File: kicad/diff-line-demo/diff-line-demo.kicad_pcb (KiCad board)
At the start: 4 copper layers, 120 x 120 mm, 2 parts, among them J1 HDMI_A, J2 HDMI_A

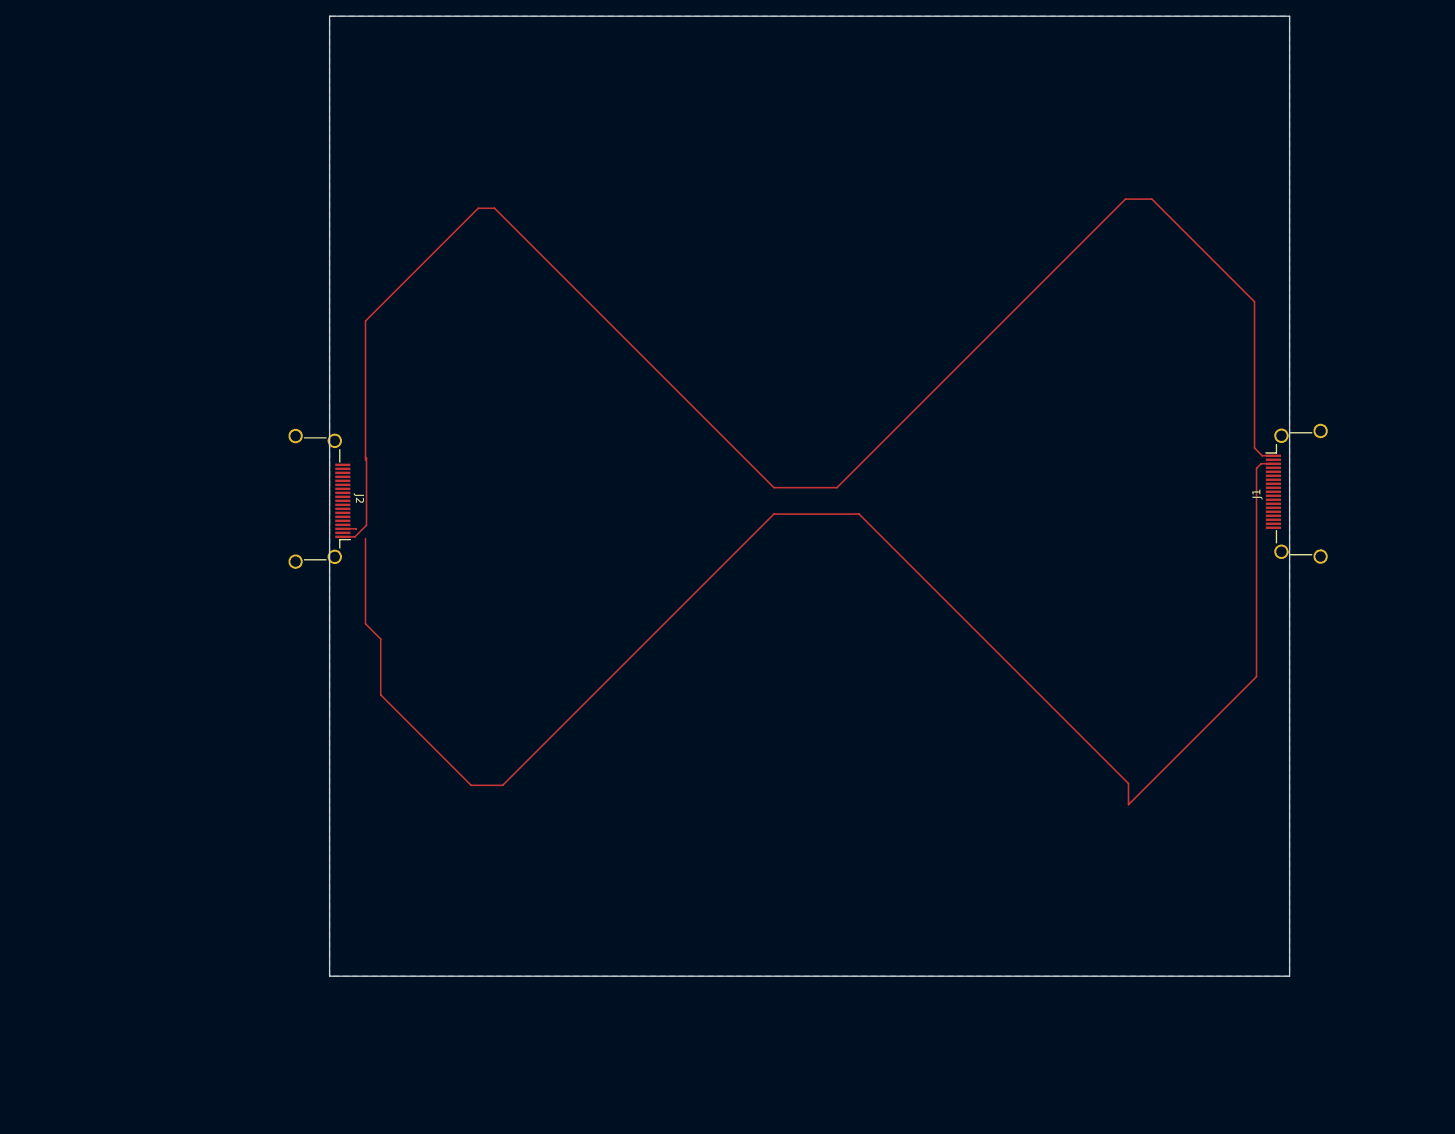
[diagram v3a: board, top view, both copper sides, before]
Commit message: Route all signals.
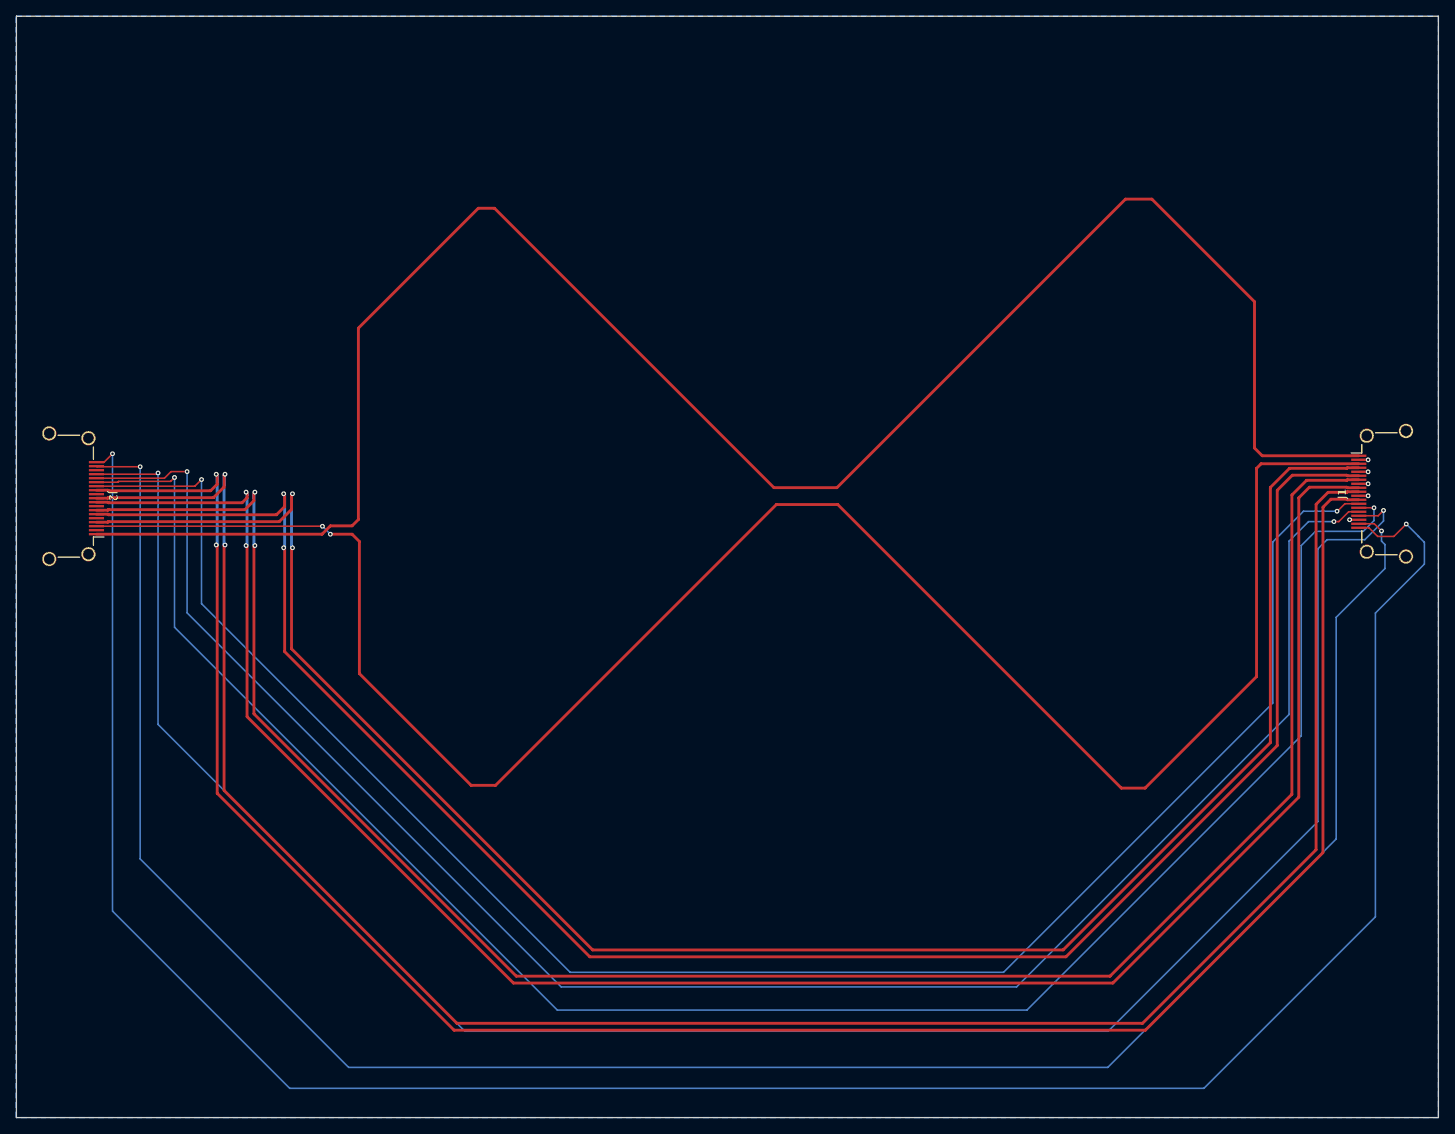
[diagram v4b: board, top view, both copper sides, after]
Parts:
- moved J2 30.8 mm to (55.9, 100.0)
- moved J1 10.7 mm to (223.6, 99.7)
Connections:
- net Net-(J1-D0+) renamed /D0+
- net Net-(J1-D0-) renamed /D0-
- net Net-(J1-D1+) renamed /D1+
- net Net-(J1-D1-) renamed /D1-
- J1 pad 10: unconnected-(J1-CK+-Pad10) -> /CK+
- J1 pad 11: unconnected-(J1-CKS-Pad11) -> GND
- J1 pad 12: unconnected-(J1-CK--Pad12) -> /CK-
- J1 pad 13: unconnected-(J1-CEC-Pad13) -> Net-(J1-CEC)
- J1 pad 14: unconnected-(J1-UTILITY-Pad14) -> Net-(J1-UTILITY)
- J1 pad 15: unconnected-(J1-SCL-Pad15) -> Net-(J1-SCL)
- J1 pad 16: unconnected-(J1-SDA-Pad16) -> Net-(J1-SDA)
- J1 pad 17: unconnected-(J1-GND-Pad17) -> GND
- J1 pad 18: unconnected-(J1-+5V-Pad18) -> Net-(J1-+5V)
- J1 pad 19: unconnected-(J1-HPD-Pad19) -> Net-(J1-HPD)
- J1 pad 2: unconnected-(J1-D2S-Pad2) -> GND
- J1 pad 5: unconnected-(J1-D1S-Pad5) -> GND
- J1 pad 8: unconnected-(J1-D0S-Pad8) -> GND
- J1 pad SH: unconnected-(J1-PadSH) -> GND
- J2 pad 10: unconnected-(J2-CK+-Pad10) -> /CK+
- J2 pad 11: unconnected-(J2-CKS-Pad11) -> GND
- J2 pad 12: unconnected-(J2-CK--Pad12) -> /CK-
- J2 pad 13: unconnected-(J2-CEC-Pad13) -> Net-(J1-CEC)
- J2 pad 14: unconnected-(J2-UTILITY-Pad14) -> Net-(J1-UTILITY)
- J2 pad 15: unconnected-(J2-SCL-Pad15) -> Net-(J1-SCL)
- J2 pad 16: unconnected-(J2-SDA-Pad16) -> Net-(J1-SDA)
- J2 pad 17: unconnected-(J2-GND-Pad17) -> GND
- J2 pad 18: unconnected-(J2-+5V-Pad18) -> Net-(J1-+5V)
- J2 pad 19: unconnected-(J2-HPD-Pad19) -> Net-(J1-HPD)
- J2 pad 2: unconnected-(J2-D2S-Pad2) -> GND
- J2 pad 5: unconnected-(J2-D1S-Pad5) -> GND
- J2 pad 8: unconnected-(J2-D0S-Pad8) -> GND
- J2 pad SH: unconnected-(J2-PadSH) -> GND
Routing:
- net Net-(J1-HPD): track 0.00 -> 295.1 mm, vias 0 -> 2
- net Net-(J1-+5V): track 0.00 -> 271.1 mm, vias 0 -> 2
- net /CK+: track 0.00 -> 264.6 mm, vias 0 -> 2
- net /CK-: track 0.00 -> 264.6 mm, vias 0 -> 2
- net Net-(J1-SDA): track 0.00 -> 259.3 mm, vias 0 -> 2
- net /D0-: track 0.00 -> 248.5 mm, vias 0 -> 2
- net /D0+: track 0.00 -> 248.5 mm, vias 0 -> 2
- net Net-(J1-UTILITY): track 0.00 -> 241.3 mm, vias 0 -> 2
- net /D1+: track 0.00 -> 239.2 mm, vias 0 -> 2
- net /D1-: track 0.00 -> 239.2 mm, vias 0 -> 2
- net Net-(J1-SCL): track 0.00 -> 232.5 mm, vias 0 -> 2
- net Net-(J1-CEC): track 0.00 -> 228.8 mm, vias 0 -> 2
- net Net-(J1-D2-): track 201.9 -> 242.1 mm, vias 0 -> 2
- net Net-(J1-D2+): track 202.3 -> 242.1 mm
- net GND: track 0.00 -> 5.82 mm, vias 0 -> 5
- added copper zone on B.Cu, net GND
- added copper zone on In1.Cu, net GND
- added copper zone on In2.Cu, net GND
- removed copper zone on B.Cu, net (none)
- removed copper zone on In1.Cu, net (none)
- removed copper zone on In2.Cu, net (none)
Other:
- board size 120 x 120 mm -> 177.7 x 137.7 mm
